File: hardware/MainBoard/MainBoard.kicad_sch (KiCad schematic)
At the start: 49 parts, among them J1 Conn_01x08_Socket, J2 Conn_01x08_Socket, J3 Conn_01x08_Socket, J4 Micro_SD_Card_Det2, J5 USB_C_Receptacle_USB2.0_16P, J6 LIPO GND, J7 LIPO PWR, J8 En_A, J9 En_B, Q1 MMBT2222A, U1 ESP32-S3-WROOM-1, U2 AMS1117-3.3, U3 AMS1117-5.0

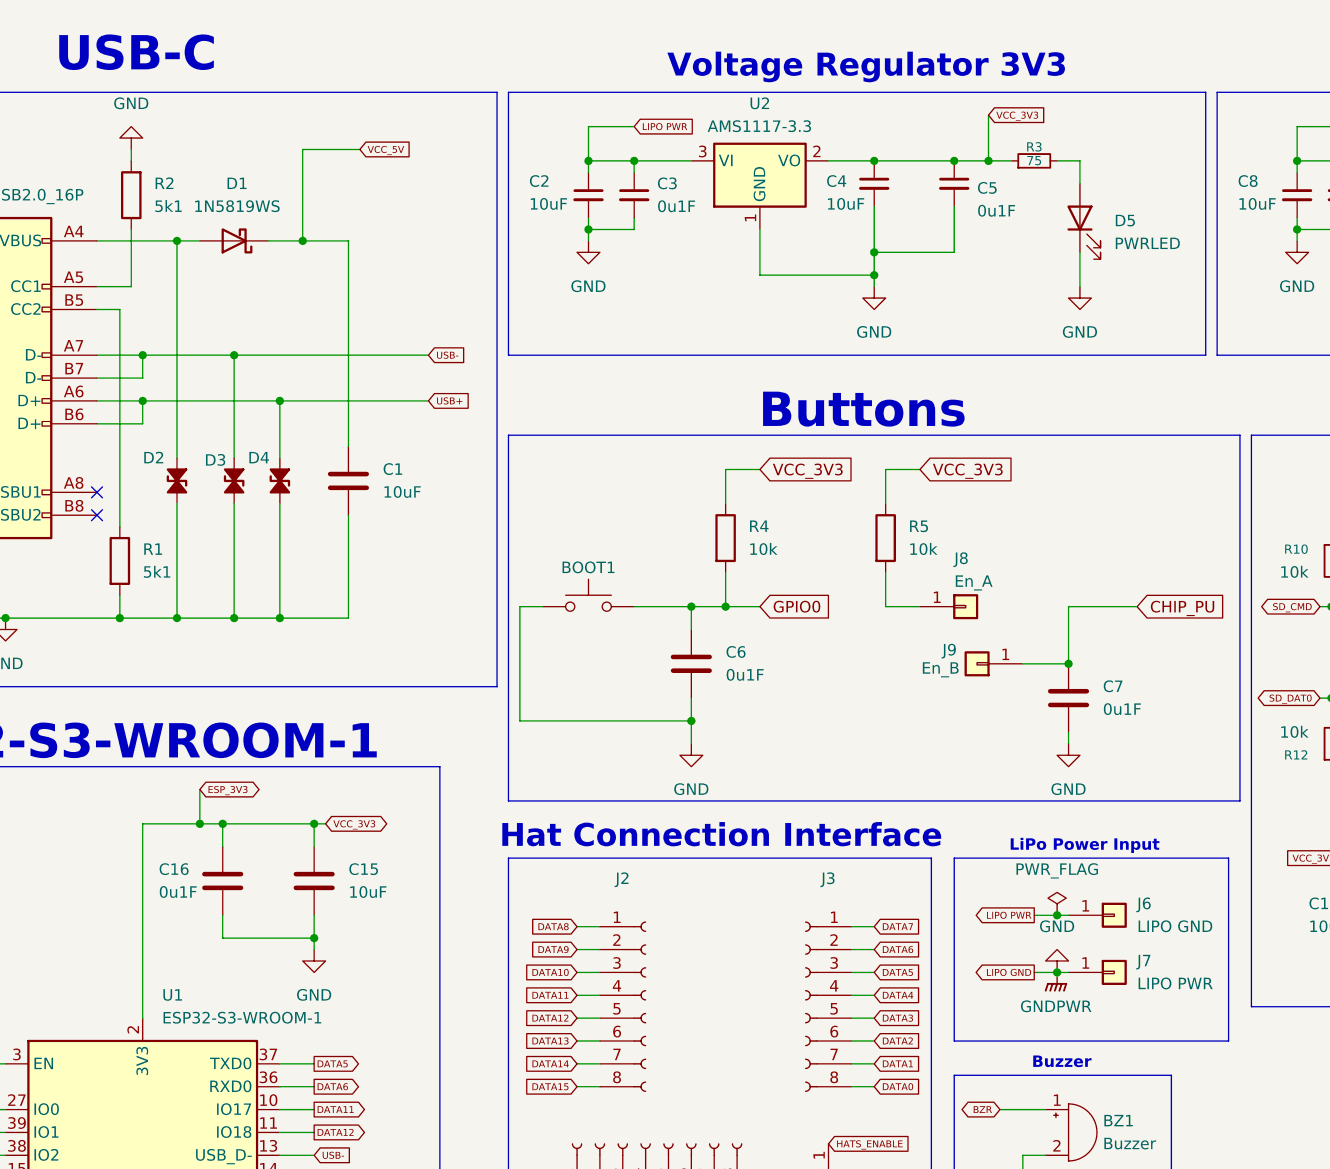
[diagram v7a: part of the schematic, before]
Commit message: added power from usb to main board
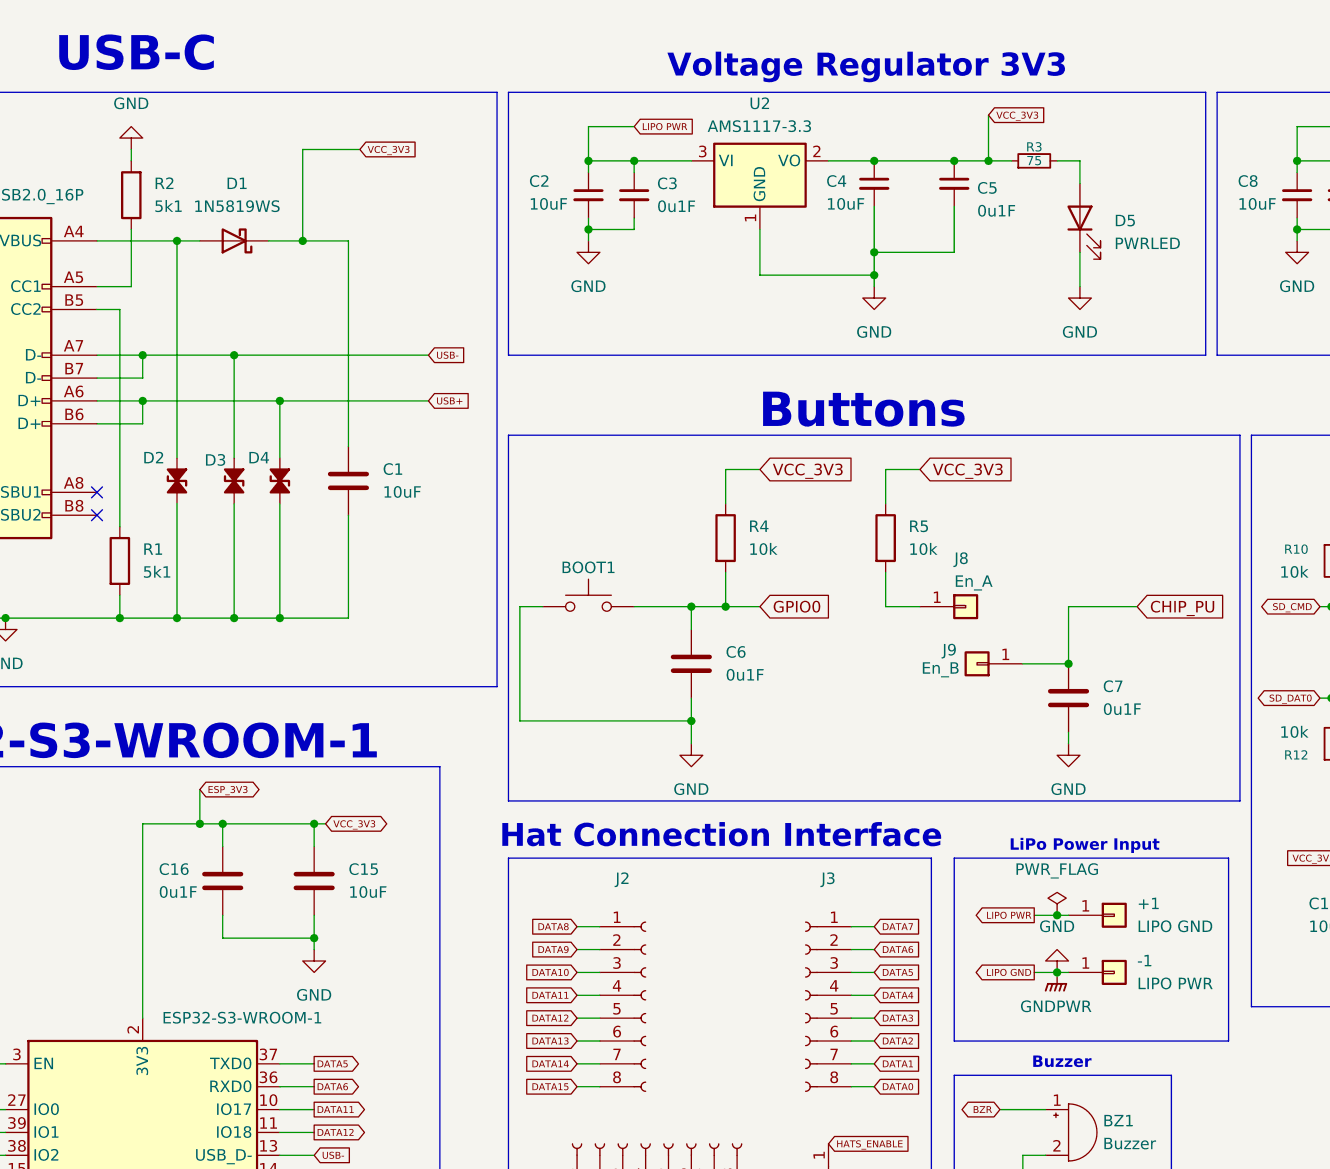
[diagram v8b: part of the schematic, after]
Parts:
- renumbered J6 to +1, J7 to -1
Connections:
- net ESP_3V3: now also C1.1, D1.1 (K)
- net VCC_5V: no longer C1.1, D1.1 (K)
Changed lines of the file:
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@@
 		)
 	)
-	(global_label "VCC_5V"
+	(global_label "VCC_3V3"
 		(shape input)
 		(at 81.28 26.67 0)
@@
 		)
 		(property "Intersheetrefs" "${INTERSHEET_REFS}"
-			(at 87.2079 26.67 0)
+			(at 87.9336 26.67 0)
 			(effects
 				(font
@@
 		(dnp no)
 		(fields_autoplaced yes)
-		(property "Reference" "J6"
+		(property "Reference" "+1"
 			(at 167.64 110.4899 0)
 			(effects
@@
 			(project ""
 				(path "/988df97c-fca1-40e2-af98-331e3f3f354f"
-					(reference "J6")
+					(reference "+1")
 					(unit 1)
 				)
@@
 		(dnp no)
 		(fields_autoplaced yes)
-		(property "Reference" "J7"
+		(property "Reference" "-1"
 			(at 167.64 116.8399 0)
 			(effects
@@
 			(project ""
 				(path "/988df97c-fca1-40e2-af98-331e3f3f354f"
-					(reference "J7")
+					(reference "-1")
 					(unit 1)
 				)
@@
 				)
 				(justify left)
+				(hide yes)
 			)
 		)
